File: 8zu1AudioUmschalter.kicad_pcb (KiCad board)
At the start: 2 copper layers, 56 parts, among them IC1 ATMEGA8A-A, IC2 MAX9890, J1 USB, J2 LUM 1503-07, J3 LUM 1503-07, J4 LUM 1503-07, J5 LUM 1503-07, J6 LUM 1503-07, J7 LUM 1503-07, J8 LUM 1503-07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

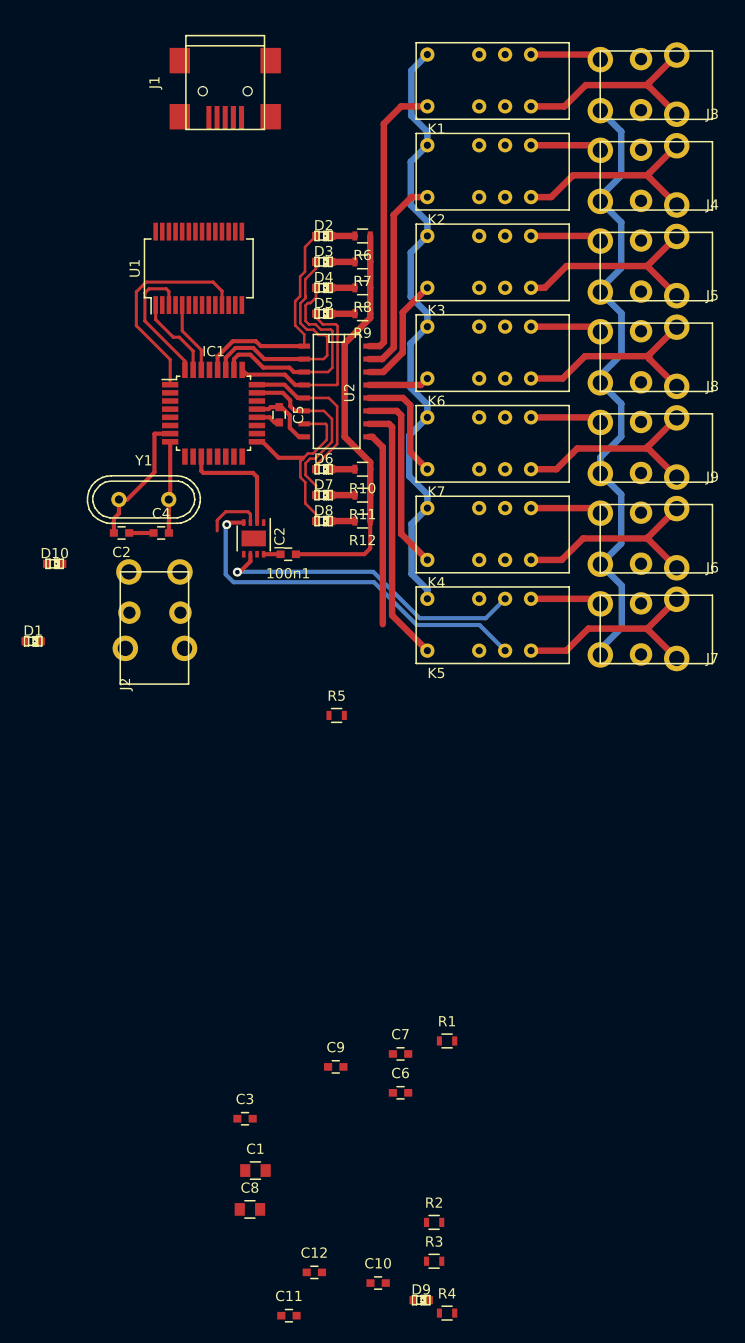
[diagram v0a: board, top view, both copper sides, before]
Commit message: Erste vollständige PCB ohne Masseflächen
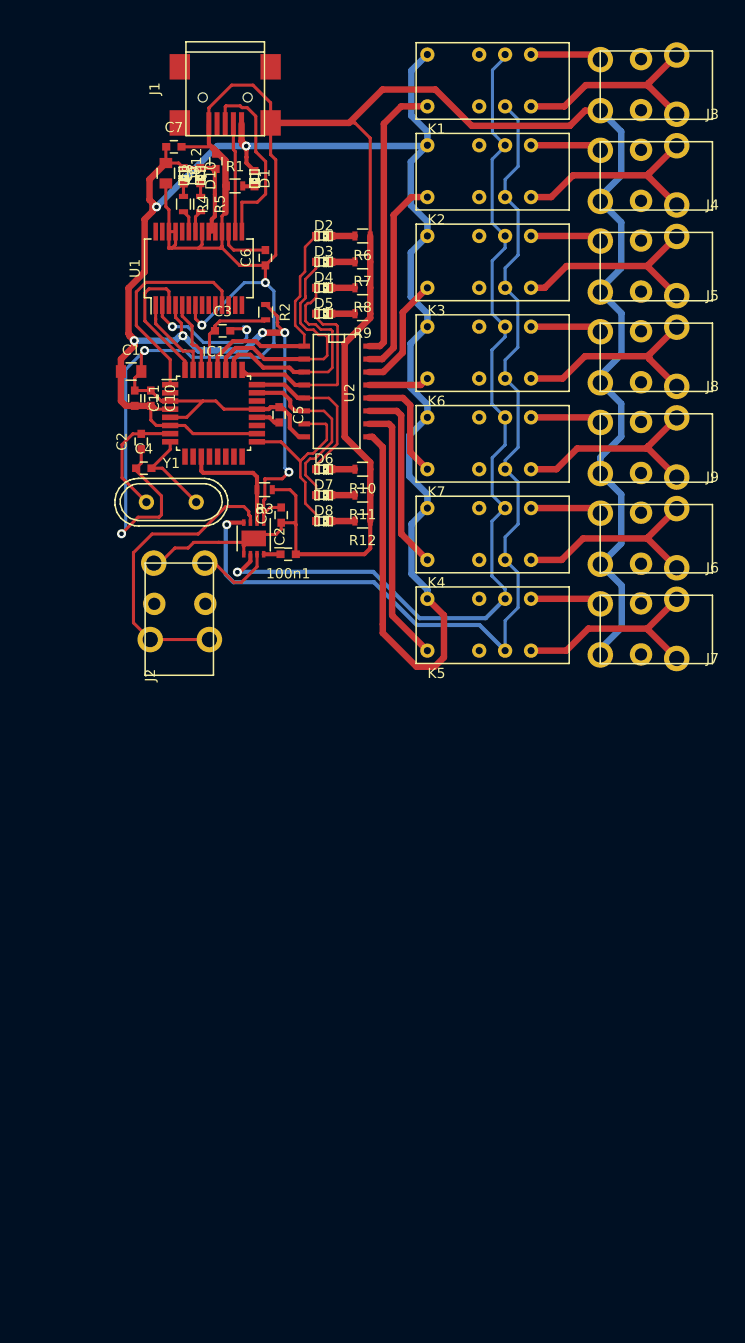
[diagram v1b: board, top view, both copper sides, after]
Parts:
- moved D9 112.6 mm to (141.2, 76.7), turned to 270 degrees
- moved R4 111.7 mm to (141.2, 79.4), turned to 270 degrees
- moved C12 109.3 mm to (144.4, 75.2), turned to 90 degrees
- moved C8 101.9 mm to (139.5, 76.4), turned to 270 degrees
- moved C7 91.6 mm to (140.3, 73.8)
- moved C11 91.2 mm to (136.4, 98.5), turned to 270 degrees
- moved R2 90.7 mm to (149.3, 90.0), turned to 270 degrees
- moved C10 89.5 mm to (138.0, 98.5), turned to 270 degrees
- moved R1 86.3 mm to (146.3, 77.6)
- moved C6 82.9 mm to (149.2, 84.7), turned to 90 degrees
- moved C1 79.3 mm to (136.1, 95.8)
- moved R3 77.4 mm to (149.1, 107.4), turned to 180 degrees
- moved C3 77.2 mm to (145.0, 91.8)
- moved C9 54.3 mm to (150.8, 109.9), turned to 90 degrees
- moved R5 51.9 mm to (142.9, 79.4), turned to 270 degrees
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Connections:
- C12 pad 1: Net-(C12-Pad1) -> VCC
- C12 pad 2: Net-(C12-Pad2) -> GND
- C7 pad 1: Net-(C12-Pad1) -> VCC
- C7 pad 2: Net-(C12-Pad2) -> GND
- IC2 pad 9: (no net) -> GND
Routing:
- net GND: track 112.9 -> 340.6 mm, vias 0 -> 4
- net VCC: track 80.6 -> 239.3 mm, vias 0 -> 7
- net /CH_R_REL_IN: track 31.3 -> 91.0 mm
- net /CH_L_REL_IN: track 37.1 -> 96.8 mm
- net Net-(IC2-Pad3): track 5.57 -> 29.5 mm
- net Net-(J1-Pad3): track 0.00 -> 18.7 mm
- net /DTR: track 0.00 -> 13.7 mm, vias 0 -> 2
- net Net-(J1-Pad2): track 0.00 -> 10.6 mm
- net Net-(C3-Pad1): track 0.00 -> 9.96 mm
- net Net-(IC2-Pad7): track 0.00 -> 7.79 mm
- net Net-(C6-Pad2): track 0.00 -> 5.12 mm
- net Net-(R4-Pad2): track 0.00 -> 2.17 mm
- net Net-(R5-Pad2): track 0.00 -> 2.16 mm
- net Net-(C2-Pad2): track 13.4 -> 11.8 mm
- net Net-(D10-Pad2): track 0.00 -> 1.31 mm
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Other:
- net class Default: clearance 0.254 -> 0.2
- rule trace_clearance: 0.254 -> 0.2
- rule trace_min: 0.254 -> 0.2

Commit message: Platine nun 59 x 80 um den Abstand zwischen den 3.5 mm Buchsen zu vergrößern
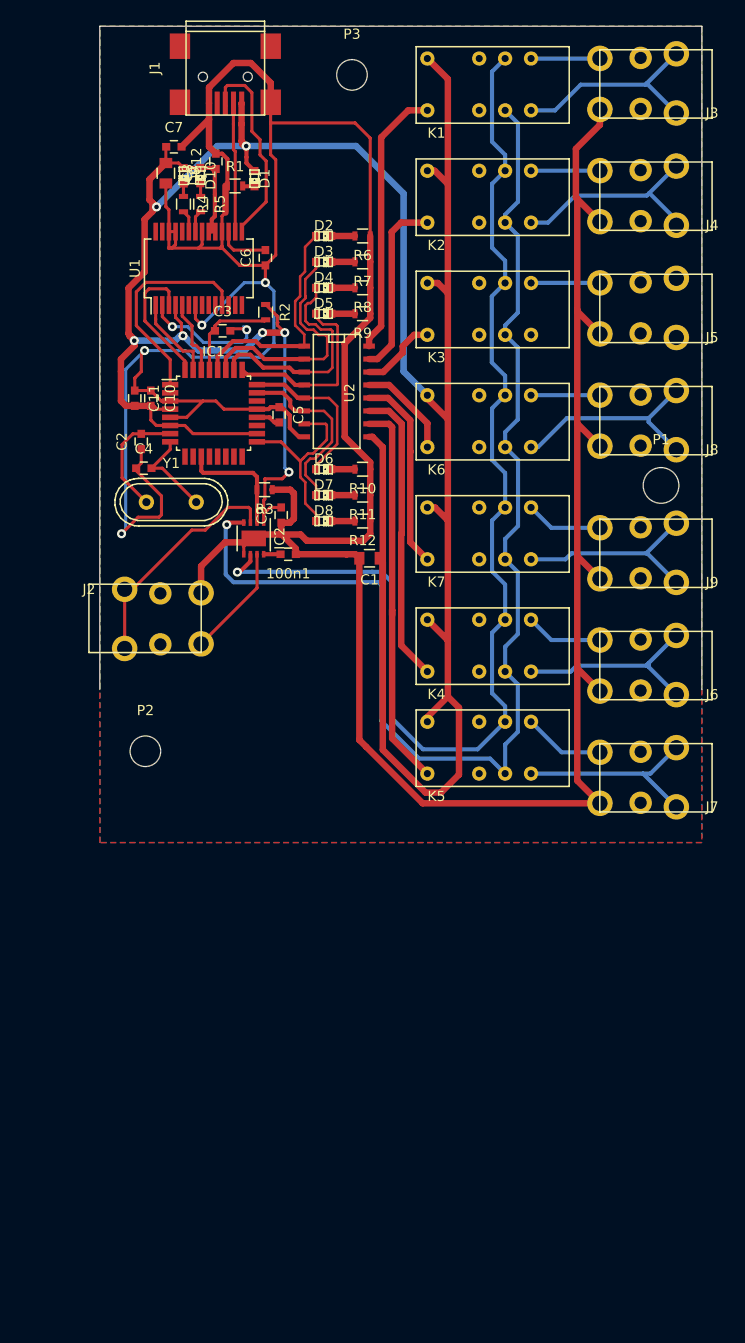
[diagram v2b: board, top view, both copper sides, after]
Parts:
- added P1: CONN_01X01, Mounting_Holes:MountingHole_3-5mm, F.Cu at (188.0, 107.0)
- added P2: CONN_01X01, Mounting_Holes:MountingHole_3mm, F.Cu at (137.5, 133.0)
- added P3: CONN_01X01, Mounting_Holes:MountingHole_3mm, F.Cu at (157.7, 66.8)
- moved C1 29.7 mm to (159.4, 114.1), turned to 180 degrees
- moved J7 14.5 mm to (193.0, 139.0)
- moved J6 12.4 mm to (193.0, 128.0)
- moved K5 12.0 mm to (164.0, 129.0)
- moved K4 10.9 mm to (164.0, 119.0)
- moved J2 10.5 mm to (131.9, 116.7), turned to 0 degrees
- moved J9 10.3 mm to (193.0, 117.0)
- moved K7 8.83 mm to (164.0, 108.0)
- moved K6 6.72 mm to (164.0, 97.0)
- moved J8 6.21 mm to (193.0, 104.0)
- moved K3 4.61 mm to (164.0, 86.0)
- moved J5 4.10 mm to (193.0, 93.0)
- moved K2 2.50 mm to (164.0, 75.0)
- moved J1 2.02 mm to (145.3, 66.1)
- moved J4 1.99 mm to (193.0, 82.0)
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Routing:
- net VCC: track 239.3 -> 298.5 mm
- net GND: track 340.6 -> 380.2 mm
- net /CH_R_REL_IN: track 91.0 -> 116.4 mm
- net /CH_L_REL_IN: track 96.8 -> 121.1 mm
- net Net-(J5-Pad2): track 20.5 -> 0.00 mm
- net Net-(K5-Pad9): track 25.7 -> 38.3 mm
- net Net-(K4-Pad9): track 18.6 -> 29.1 mm
- net Net-(K7-Pad9): track 11.3 -> 19.4 mm
- net Net-(IC2-Pad3): track 29.5 -> 22.8 mm
- net Net-(K3-Pad9): track 11.4 -> 7.59 mm
- net Net-(K6-Pad9): track 5.98 -> 9.60 mm
- net Net-(IC2-Pad7): track 7.79 -> 11.1 mm
- net Net-(IC1-Pad11): track 11.6 -> 14.8 mm
- net Net-(K2-Pad9): track 19.9 -> 17.7 mm
- net Net-(J1-Pad2): track 10.6 -> 12.7 mm
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- added copper zone on B.Cu, net GND
- added copper zone on F.Cu, net GND
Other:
- board outline added: 59 x 65 mm

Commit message: Kleinere Änderungen und Hinzufügen des TMP75
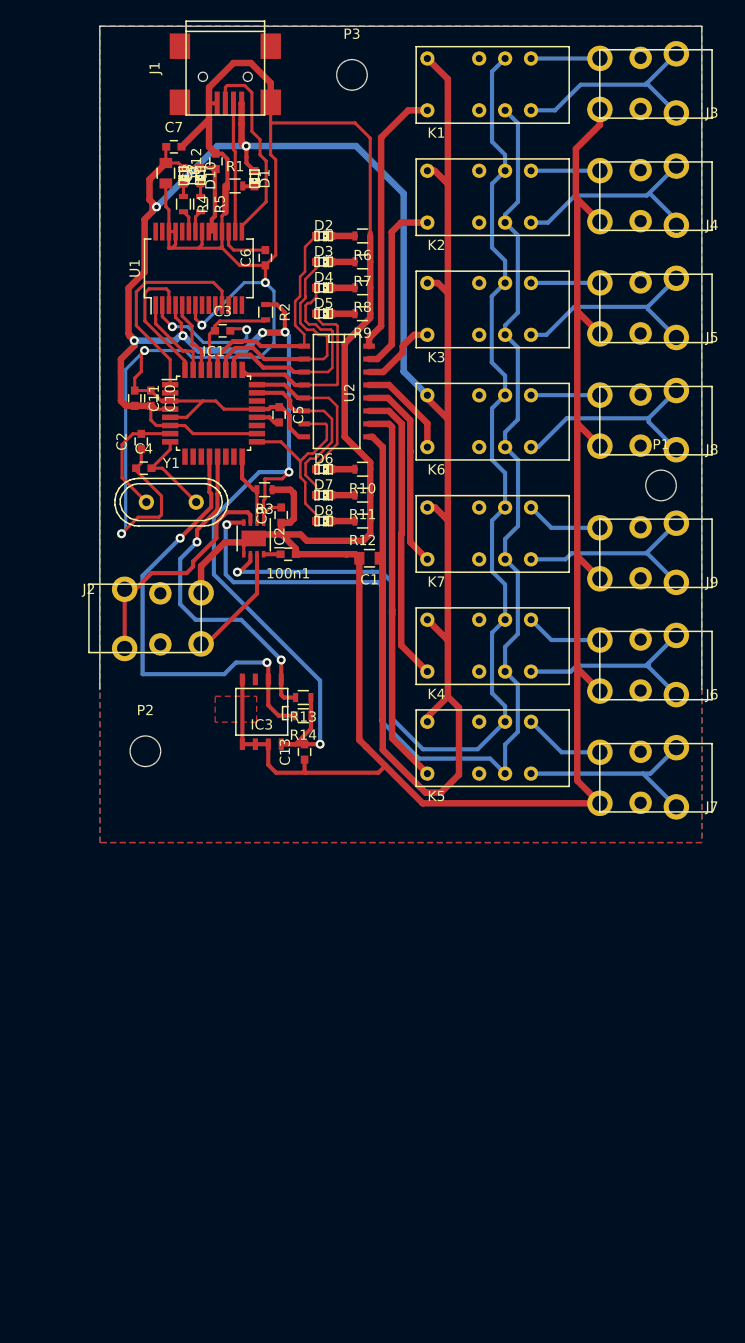
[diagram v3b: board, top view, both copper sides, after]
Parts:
- added C13: 100n, Capacitors_SMD:C_0603, F.Cu at (153.1, 133.1)
- added IC3: TMP75, SMD_Packages:SOIC-8-N, F.Cu at (148.9, 129.2)
- added R13: 5k, Resistors_SMD:R_0603, F.Cu at (152.9, 127.8)
- added R14: 5k, Resistors_SMD:R_0603, F.Cu at (152.9, 129.6)
- P1: footprint Mounting_Holes:MountingHole_3-5mm -> Mounting_Holes:MountingHole_3mm
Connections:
- IC1 pad 12: Net-(IC1-Pad12) -> /SCL
- IC1 pad 13: Net-(IC1-Pad13) -> /SDA
- IC1 pad 16: Net-(IC1-Pad16) -> /MAX98_SHDN
- IC2 pad 2: Net-(IC1-Pad11) -> /MAX98_SHDN
- R3 pad 2: Net-(IC1-Pad11) -> /MAX98_SHDN
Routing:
- net VCC: track 298.5 -> 348.4 mm, vias 7 -> 8
- net /SCL: track 0.00 -> 44.2 mm, vias 0 -> 2
- net /SDA: track 0.00 -> 33.1 mm, vias 0 -> 2
- net GND: track 380.2 -> 405.3 mm
- net Net-(J5-Pad2): track 0.00 -> 20.7 mm
- net Net-(IC1-Pad11): track 14.8 -> 0.00 mm
- net /MAX98_SHDN: track 0.00 -> 7.27 mm
- net Net-(IC2-Pad3): track 22.8 -> 24.2 mm
- added copper zone on F.Cu, net VCC

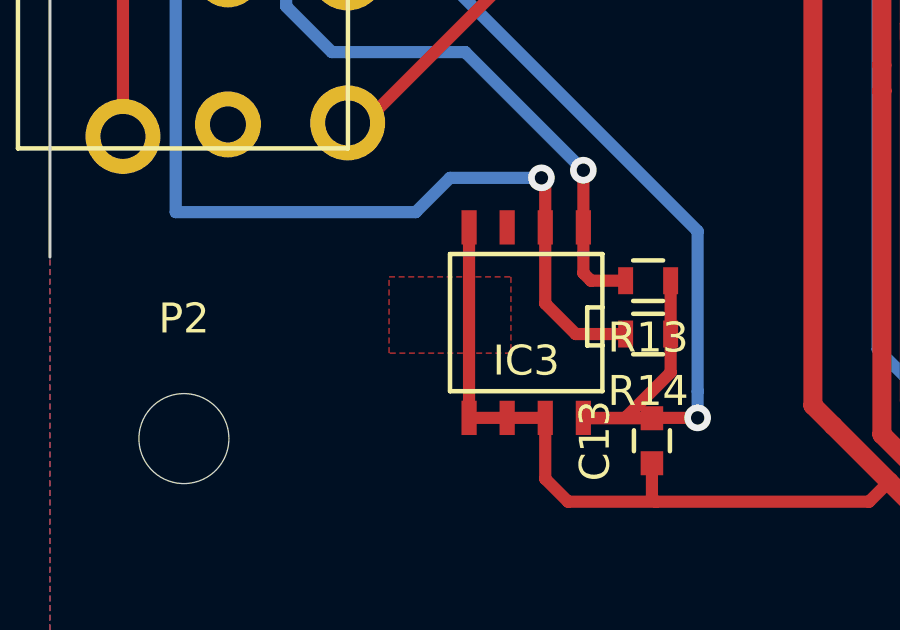
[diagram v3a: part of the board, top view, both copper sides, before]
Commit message: Massefläche unter TMP75 entfernt
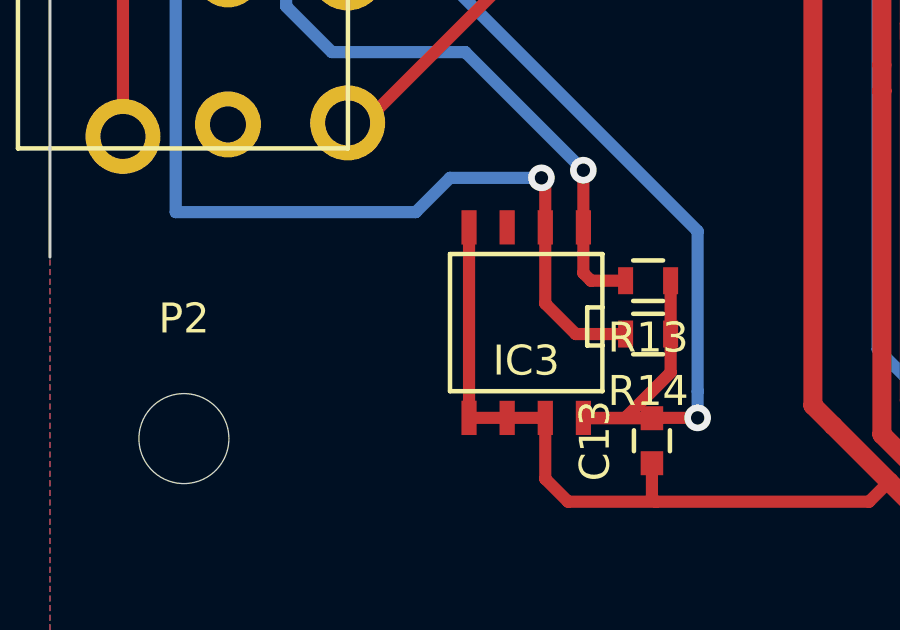
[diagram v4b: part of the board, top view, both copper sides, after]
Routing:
- removed copper zone on F.Cu, net VCC

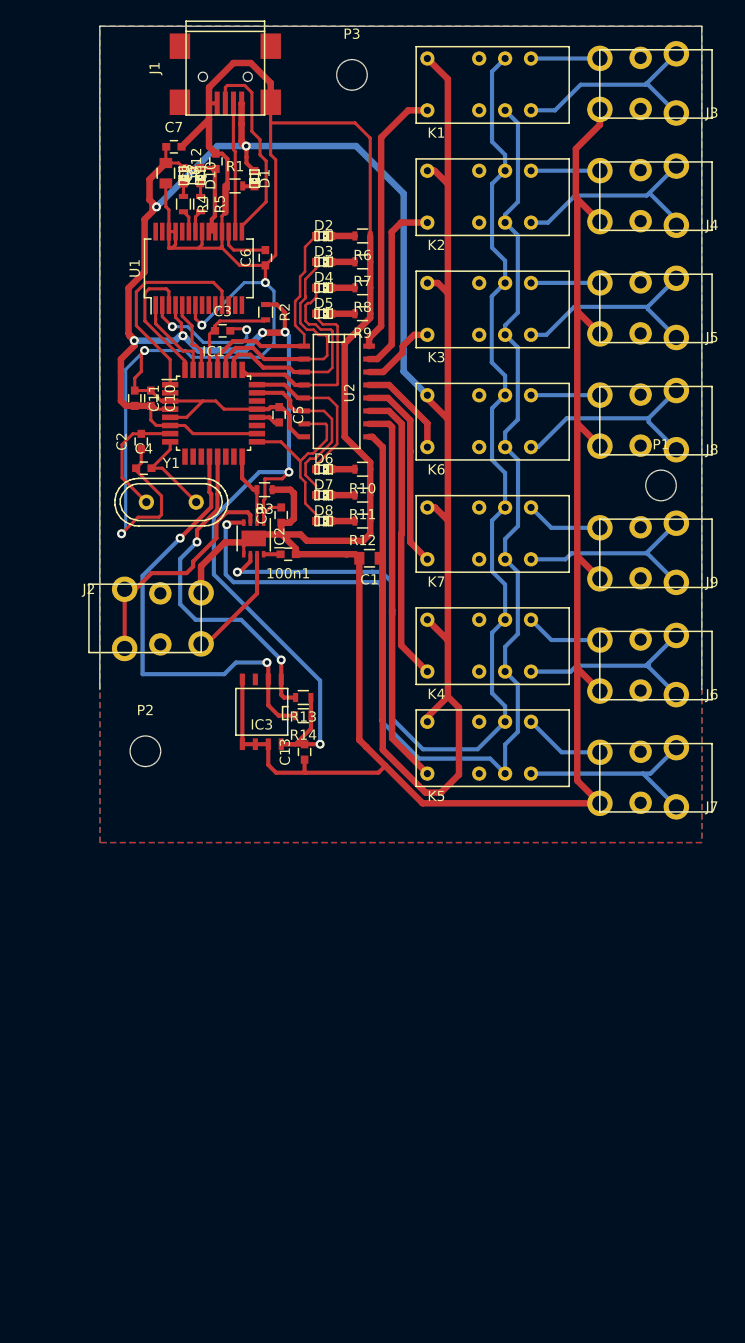
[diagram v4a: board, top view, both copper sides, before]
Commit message: Änderungen in den Masseflächen Ist es o.k. USB shield nicht mit GND zu verbinden ?
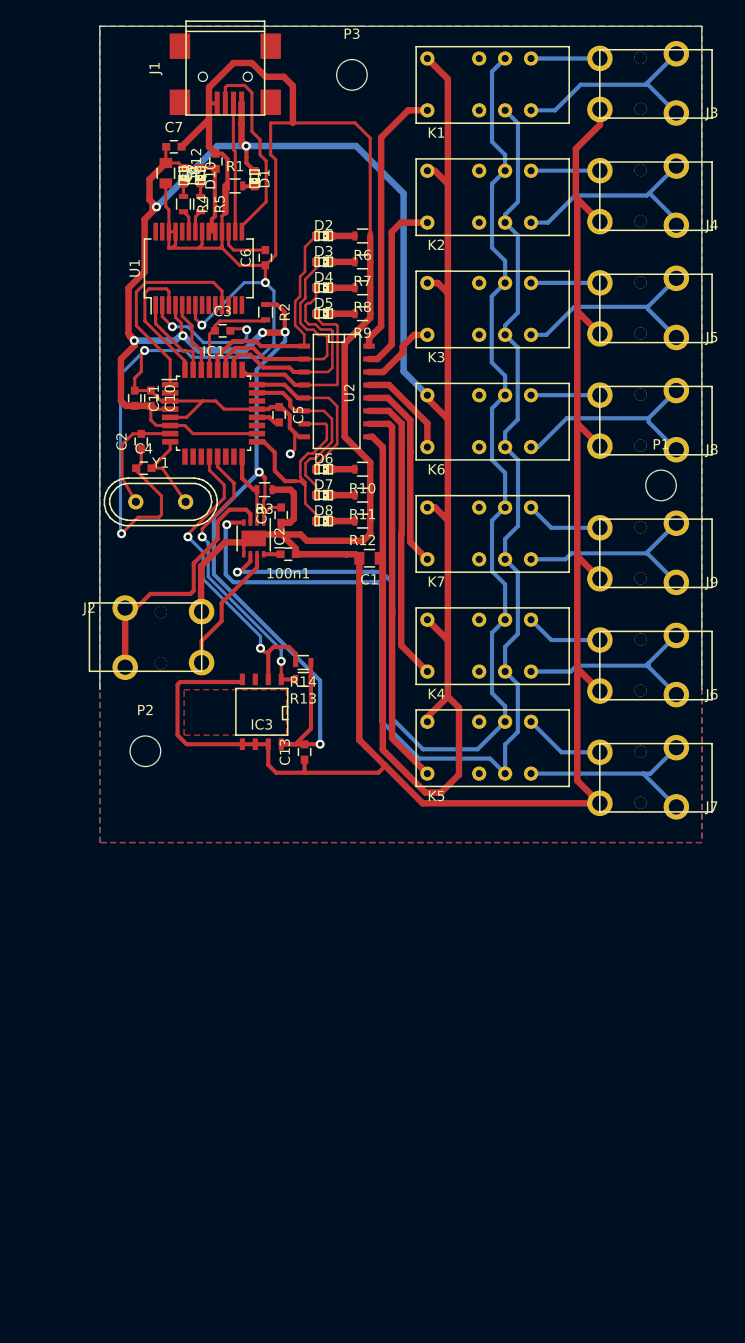
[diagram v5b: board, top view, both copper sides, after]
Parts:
- moved R14 5.21 mm to (152.9, 124.4)
- moved J2 1.84 mm to (132.0, 118.5)
- moved R13 1.78 mm to (152.9, 126.0)
- moved Y1 1.04 mm to (139.0, 108.6)
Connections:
- IC1 pad 10: Net-(IC1-Pad10) -> (no net)
- IC1 pad 11: Net-(IC1-Pad11) -> (no net)
- IC1 pad 14: Net-(IC1-Pad14) -> (no net)
- IC1 pad 15: Net-(IC1-Pad15) -> (no net)
- IC1 pad 19: Net-(IC1-Pad19) -> (no net)
- IC1 pad 2: Net-(IC1-Pad2) -> (no net)
- IC1 pad 22: Net-(IC1-Pad22) -> (no net)
- IC1 pad 9: Net-(IC1-Pad9) -> (no net)
- IC3 pad 3: Net-(IC3-Pad3) -> (no net)
- K1 pad 14: Net-(K1-Pad14) -> (no net)
- K1 pad 3: Net-(K1-Pad3) -> (no net)
- K2 pad 14: Net-(K2-Pad14) -> (no net)
- K2 pad 3: Net-(K2-Pad3) -> (no net)
- K3 pad 14: Net-(K3-Pad14) -> (no net)
- K3 pad 3: Net-(K3-Pad3) -> (no net)
- K4 pad 14: Net-(K4-Pad14) -> (no net)
- K4 pad 3: Net-(K4-Pad3) -> (no net)
- K5 pad 14: Net-(K5-Pad14) -> (no net)
- K5 pad 3: Net-(K5-Pad3) -> (no net)
- K6 pad 14: Net-(K6-Pad14) -> (no net)
- K6 pad 3: Net-(K6-Pad3) -> (no net)
- K7 pad 14: Net-(K7-Pad14) -> (no net)
- K7 pad 3: Net-(K7-Pad3) -> (no net)
- P1 pad 1: Net-(P1-Pad1) -> (no net)
- P2 pad 1: Net-(P2-Pad1) -> (no net)
- P3 pad 1: Net-(P3-Pad1) -> (no net)
- U1 pad 10: Net-(U1-Pad10) -> (no net)
- U1 pad 12: Net-(U1-Pad12) -> (no net)
- U1 pad 13: Net-(U1-Pad13) -> (no net)
- U1 pad 14: Net-(U1-Pad14) -> (no net)
- U1 pad 27: Net-(U1-Pad27) -> (no net)
- U1 pad 28: Net-(U1-Pad28) -> (no net)
- U1 pad 6: Net-(U1-Pad6) -> (no net)
- U1 pad 9: Net-(U1-Pad9) -> (no net)
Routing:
- net GND: track 405.3 -> 423.4 mm, vias 4 -> 5
- net /SCL: track 44.2 -> 31.4 mm
- net /SDA: track 33.1 -> 28.5 mm
- net /REL6: track 19.3 -> 21.8 mm
- net Net-(IC2-Pad3): track 24.2 -> 25.7 mm
- net Net-(IC2-Pad7): track 11.4 -> 12.9 mm
- net Net-(C4-Pad2): track 9.14 -> 8.45 mm
- net Net-(C2-Pad2): track 11.8 -> 11.1 mm
- added copper zone on F.Cu, net (none)
